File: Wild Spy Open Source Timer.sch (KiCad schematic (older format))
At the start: 36 parts, among them Q1 AO3415, Q2 AO3415, Q3 AO3415, Q4 AO3415, Q5 AO3415, U1 DS3232SN, U2 TPS70925DBVR, U3 UM6K33N, U4 UM6K33N, U5 ATXMEGA32C4-A

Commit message: Swapped to the d21 in the schematic
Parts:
- removed C3, C4, C6, C7: 0.1uF, Capacitors_SMD:C_0603_HandSoldering, symbol C_Small
- removed PDI1: CONN_01X04, MC_Footprint:PDI_PROG_HEADER, symbol CONN_01X04
- removed PortA1: CONN_01X10, Pin_Headers:Pin_Header_Straight_1x10, symbol CONN_01X10
- removed PortC1: CONN_01X10, MC_Footprint:5x2connnector_small, symbol CONN_01X10
- removed R3: 10k, Resistors_SMD:R_0603_HandSoldering, symbol R
- removed U5: ATXMEGA32C4-A, Housings_QFP:TQFP-44_10x10mm_Pitch0.8mm, symbol ATXMEGA32C4-A
- added C? (x2): 0.1uF, Capacitors_SMD:C_0603_HandSoldering, symbol C_Small
- added C?: 1uF, Capacitors_SMD:C_0603_HandSoldering, symbol C_Small
- added J?: CONN_01X05, Pin_Headers:Pin_Header_Straight_1x05_Pitch2.54mm, symbol CONN_01X05
- added J?: CONN_02X04, Pin_Headers:Pin_Header_Straight_2x04_Pitch2.54mm, symbol CONN_02X04
- added R?: 1.7k, Resistors_SMD:R_0603_HandSoldering, symbol R
- added R?: 3.3k, Resistors_SMD:R_0603_HandSoldering, symbol R
- added U?: ATSAMD21E16B, Housings_DFN_QFN:QFN-32-1EP_5x5mm_Pitch0.5mm, symbol ATSAMD21E16B
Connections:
- net labels added: NRESET, PA08, PA09, PA10, PA11, PA14, PA15, SWDCLK, SWDIO, USBSENSE3.3
- net labels removed: PA0, PA1, PA2, PA3, PA4, PA5, PA6, PA7, PC0, PC1, PC2, PC3, PC4, PC5, PC6, PC7, PDI_CLK, PDI_DATA
- wire segments 149 -> 100
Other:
- note removed: "Extra ports broken out."
- note removed: "needed?"

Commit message: - Updates to Rev1 Schematic - Organising/Tidying - Add peripheral bus port - Battery voltage measurement - Battery/USB selection jumper - Started skeleton of Rev1 PCB - Added libs folder with some footprints
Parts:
- removed Coin1: 16mm_Coin_Cell, MC_Footprint:CoinCell_Holder_1632, symbol 16mm_Coin_Cell
- added JP1: JUMPER3, jumper:SOLDER-JUMPER_2-WAY, symbol JUMPER3
- added PBus1: CONN_01X04, Pin_Headers:Pin_Header_Straight_1x04, symbol CONN_01X04
- added Q6: AO3415, TO_SOT_Packages_SMD:SOT-23, symbol Q_PMOS_GSD
- added R3: 150k, Resistors_SMD:R_0603_HandSoldering, symbol R
- added R8: 10k, Resistors_SMD:R_0603_HandSoldering, symbol R
- R4, R5, R6, R7: value 10k -> 100k
- U2: value TPS70925DBVR -> TPS70933DBVR; Supplier 1 Cost 1.1334 -> 1.19; Supplier 1 Part Number 296-40923-1-ND -> 296-35483-1-ND
- U5: renamed from U?; value ATSAMD21E16B -> ATSAMD21E18B; Manufacturer Part Number (none) -> ATSAMD21E18A-MUT; Supplier 1 (none) -> DigiKey; Supplier 1 Cost (none) -> 3.64; Supplier 1 Currency (none) -> AUD; Supplier 1 Part Number (none) -> 1611-ATSAMD21E18A-MUTCT-ND
- gave numbers to parts that had none: 7
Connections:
- net labels added: BAT+, PBus1_MRX, PBus1_MTX, VBat/12, ~BatMeasureEn
- wire segments 100 -> 123
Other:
- note added: "3.3V"
- note added: "Battery Voltage Measure"
- note added: "Breakout"
- note added: "Channels"
- note added: "Does it count if the USB is just not plugged in? Or\nis this ok as long as we have the USB set up?"
- note added: "From Datasheet:\nIf the PA24 and PA25 pins are not connected, \nit is recommended to enable a pull-up on PA24 and\nPA25 through input GPIO mode. The aim is to avoid \nan eventually extract power consumption (<1mA) \ndue to a not stable level on pad. The port PA24 and \nPA25 doesn't have Drive Strength option."
- note added: "Leave ID pin floating \nfor USB slave"
- note added: "MCU"
- note added: "Peripheral Bus"
- note added: "Power"
- note added: "Programming"
- note added: "RTC"
- note added: "SERCOM0/2[0]"
- note added: "SERCOM0/2[1]"
- note added: "SERCOM0/2[2]"
- note added: "SERCOM0/2[3]"
- note added: "SERCOM0[0]"
- note added: "SERCOM0[1]"
- note added: "SERCOM0[2]"
- note added: "SERCOM0[3]"
- note added: "SERCOM1/3[0]"
- note added: "SERCOM1/3[1]"
- note added: "SERCOM1/3[2]"
- note added: "SERCOM1/3[3]"
- note added: "SERCOM1[0]"
- note added: "SERCOM3/5[0]"
- note added: "SERCOM3/5[1]"
- note added: "SERCOM3/5[2]"
- note added: "SERCOM3/5[3]"
- note added: "USB"
- note removed: "Leave ID pin floating for USB slave"
- moved on the sheet: Battery1, Breakout, C1, C2, C3, C4, C5, C6, C8, CH1, CH2, CH3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

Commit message: PCB components placed
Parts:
- removed VUSB1: CONN_01X02, Pin_Headers:Pin_Header_Straight_1x02, symbol CONN_01X02
- added D1: LED, LEDs:LED_0603, symbol LED
- added R11: 1k, Resistors_SMD:R_0603_HandSoldering, symbol R
- Breakout1: renamed from Breakout; footprint Pin_Headers:Pin_Header_Straight_2x04_Pitch2.54mm -> MC_Footprint:4x2connnector_small
- PBus1: footprint Pin_Headers:Pin_Header_Straight_1x04 -> Pin_Headers:Pin_Header_Straight_1x04_Pitch2.54mm
- Q1, Q2, Q3, Q4, Q5, Q6: footprint TO_SOT_Packages_SMD:SOT-23 -> MC_Footprint:SOT-23-HandSoldering
- SWD1: renamed from SWD; footprint Pin_Headers:Pin_Header_Straight_1x05_Pitch2.54mm -> MC_Footprint:SWD_PROG_HEADER
- U1: footprint Housings_SOIC:SOIC-20_7.5x12.8mm_Pitch1.27mm -> Housings_SOIC:SOIC-20W_7.5x12.8mm_Pitch1.27mm
- U2: footprint TO_SOT_Packages_SMD:SOT-23-5 -> TO_SOT_Packages_SMD:SOT-23-5_HandSoldering
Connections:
- net labels added: LED, VBat/15
- net labels removed: VBat/12
- wire segments 123 -> 126
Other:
- note added: "LED Connected to PA07\n"
- moved on the sheet: C3

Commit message: Cleaned up routing on PCB a bit. Made some changes to schematic, added a few things.
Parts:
- removed Breakout1: CONN_02X04, MC_Footprint:4x2connnector_small, symbol CONN_02X04
- removed JP1: JUMPER3, jumper:SOLDER-JUMPER_2-WAY, symbol JUMPER3
- removed U5: ATSAMD21E18B, Housings_DFN_QFN:QFN-32-1EP_5x5mm_Pitch0.5mm, symbol ATSAMD21E16B
- added JP1: JUMPER3-closed, OSTFootprints:SOLDER-JUMPER_2-WAY-CLOSED, symbol JUMPER3-closed
- added SW1: SW_PUSH, OSTFootprints:KMT071NGJLHS_3x2.6mm_switch, symbol SW_PUSH
- added SW?: ORD213, OSTFootprints:ORD213S-1, symbol ORD213
- added U?: ATSAMD21E16B, OSTFootprints:QFN-32-1EP_5x5mm_Pitch0.5mm, symbol ATSAMD21E16B
- D1: symbol LED -> LED-RESCUE-Wild_Spy_Open_Source_Timer
- Q1, Q2, Q3, Q4, Q5, Q6: footprint MC_Footprint:SOT-23-HandSoldering -> OSTFootprints:SOT-23-HandSoldering
- SWD1: footprint MC_Footprint:SWD_PROG_HEADER -> OSTFootprints:SWD_PROG_HEADER
- U1: footprint Housings_SOIC:SOIC-20W_7.5x12.8mm_Pitch1.27mm -> OSTFootprints:SOIC-20_7.5x12.8mm_Pitch1.27mm
- U2: footprint TO_SOT_Packages_SMD:SOT-23-5_HandSoldering -> OSTFootprints:SOT-23-5_HandSoldering
- USB1: footprint MC_Footprint:micro_USB -> OSTFootprints:micro_USB
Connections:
- net labels added: BL_FW_UPDATE, REEDSW
- net labels removed: PA11, PA14, PA15
- wire segments 126 -> 129
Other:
- note removed: "Breakout"
- moved on the sheet: D1, R11

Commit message: Pretty much finished REV1 PCB. Just need to have a quick look over it and export gerbers etc.
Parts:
- removed JP1: JUMPER3-closed, OSTFootprints:SOLDER-JUMPER_2-WAY-CLOSED, symbol JUMPER3-closed
- added JP1: JUMPER3, OSTFootprints:SOLDER-JUMPER_2-WAY, symbol JUMPER3
- PBus1: footprint Pin_Headers:Pin_Header_Straight_1x04_Pitch2.54mm -> OSTFootprints:Pin_Header_Straight_1x04_Pitch2.54mm
- SWD1: footprint OSTFootprints:SWD_PROG_HEADER -> OSTFootprints:SWD_PROG_HEADER_L
- gave numbers to parts that had none: 2
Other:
- moved on the sheet: U3B, U4A
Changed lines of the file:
@@
 L UM6K33N U4
 U 1 1 5803421A
-P 9250 1550
-F 0 "U4" H 9450 1550 60  0000 C CNN
-F 1 "UM6K33N" H 9550 1600 60  0001 C CNN
-F 2 "MC_Footprint:SC88(SOT363)" H 9450 2050 60  0001 C CNN
-F 3 "http://rohmfs.rohm.com/en/products/databook/datasheet/discrete/transistor/mosfet/um6k33n.pdf" H 9800 2250 60  0001 C CNN
-F 4 "DigiKey" H 9350 1850 60  0001 C CNN "Supplier 1"
-F 5 "UM6K33NTNTR-ND" H 9450 1950 60  0001 C CNN "Supplier 1 Part Number"
-F 6 "$0.08638" H 9550 2050 60  0001 C CNN "Supplier 1 Cost"
-F 7 "AUD" H 9650 2150 60  0001 C CNN "Supplier 1 Currency"
-	1    9250 1550
+P 7350 2650
+F 0 "U4" H 7550 2650 60  0000 C CNN
+F 1 "UM6K33N" H 7650 2700 60  0001 C CNN
+F 2 "MC_Footprint:SC88(SOT363)" H 7550 3150 60  0001 C CNN
+F 3 "http://rohmfs.rohm.com/en/products/databook/datasheet/discrete/transistor/mosfet/um6k33n.pdf" H 7900 3350 60  0001 C CNN
+F 4 "DigiKey" H 7450 2950 60  0001 C CNN "Supplier 1"
+F 5 "UM6K33NTNTR-ND" H 7550 3050 60  0001 C CNN "Supplier 1 Part Number"
+F 6 "$0.08638" H 7650 3150 60  0001 C CNN "Supplier 1 Cost"
+F 7 "AUD" H 7750 3250 60  0001 C CNN "Supplier 1 Currency"
+	1    7350 2650
 	1    0    0    -1
 $EndComp
@@
 L UM6K33N U3
 U 2 1 580347ED
-P 7350 2650
-F 0 "U3" H 7550 2650 60  0000 C CNN
-F 1 "UM6K33N" H 7650 2700 60  0001 C CNN
-F 2 "MC_Footprint:SC88(SOT363)" H 7550 3150 60  0001 C CNN
-F 3 "http://rohmfs.rohm.com/en/products/databook/datasheet/discrete/transistor/mosfet/um6k33n.pdf" H 7900 3350 60  0001 C CNN
-F 4 "DigiKey" H 7450 2950 60  0001 C CNN "Supplier 1"
-F 5 "UM6K33NTNTR-ND" H 7550 3050 60  0001 C CNN "Supplier 1 Part Number"
-F 6 "$0.08638" H 7650 3150 60  0001 C CNN "Supplier 1 Cost"
-F 7 "AUD" H 7750 3250 60  0001 C CNN "Supplier 1 Currency"
-	2    7350 2650
+P 9250 1550
+F 0 "U3" H 9450 1550 60  0000 C CNN
+F 1 "UM6K33N" H 9550 1600 60  0001 C CNN
+F 2 "MC_Footprint:SC88(SOT363)" H 9450 2050 60  0001 C CNN
+F 3 "http://rohmfs.rohm.com/en/products/databook/datasheet/discrete/transistor/mosfet/um6k33n.pdf" H 9800 2250 60  0001 C CNN
+F 4 "DigiKey" H 9350 1850 60  0001 C CNN "Supplier 1"
+F 5 "UM6K33NTNTR-ND" H 9450 1950 60  0001 C CNN "Supplier 1 Part Number"
+F 6 "$0.08638" H 9550 2050 60  0001 C CNN "Supplier 1 Cost"
+F 7 "AUD" H 9650 2150 60  0001 C CNN "Supplier 1 Currency"
+	2    9250 1550
 	1    0    0    -1
 $EndComp
@@
 	1    0    0    -1
 $EndComp
-Text Label 5650 2500 0    60   ~ 0
+Text Label 5650 2400 0    60   ~ 0
 ~RTC_PEN
-Text Label 5650 2400 0    60   ~ 0
+Text Label 3950 2600 2    60   ~ 0
 RTC_~INT
 Text Label 5650 2100 0    60   ~ 0
@@
 F 0 "SWD1" H 2300 6650 50  0000 C CNN
 F 1 "CONN_01X05" V 2400 6350 50  0000 C CNN
-F 2 "OSTFootprints:SWD_PROG_HEADER" H 2300 6350 50  0001 C CNN
+F 2 "OSTFootprints:SWD_PROG_HEADER_L" H 2300 6350 50  0001 C CNN
 F 3 "" H 2300 6350 50  0001 C CNN
 	1    2300 6350
@@
 3.3V
 $Comp
-L +5V #PWR038
+L +5V #PWR036
 U 1 1 590F6CEC
 P 1650 3900
-F 0 "#PWR038" H 1650 3750 50  0001 C CNN
+F 0 "#PWR036" H 1650 3750 50  0001 C CNN
 F 1 "+5V" H 1650 4050 50  0000 C CNN
 F 2 "" H 1650 3900 50  0000 C CNN
@@
 Text Notes 3100 4800 0    60   ~ 12
 Does it count if the USB is just not plugged in? Or\nis this ok as long as we have the USB set up?
-Text Notes 4650 3850 1    40   ~ 0
+Text Notes 4650 3900 1    40   ~ 0
 SERCOM0/2[0]
-Text Notes 4750 3850 1    40   ~ 0
+Text Notes 4750 3900 1    40   ~ 0
 SERCOM0/2[1]
-Text Notes 4850 3850 1    40   ~ 0
+Text Notes 4850 3900 1    40   ~ 0
 SERCOM0/2[2]
-Text Notes 4950 3850 1    40   ~ 0
+Text Notes 4950 3900 1    40   ~ 0
 SERCOM0/2[3]
 Text Notes 3550 2400 2    40   ~ 0
@@
 $EndComp
 $Comp
-L GND #PWR039
+L GND #PWR037
 U 1 1 5911D86F
 P 1050 7250
-F 0 "#PWR039" H 1050 7000 50  0001 C CNN
+F 0 "#PWR037" H 1050 7000 50  0001 C CNN
 F 1 "GND" H 1050 7100 50  0000 C CNN
 F 2 "" H 1050 7250 50  0000 C CNN
@@
 Text Label 750  6950 1    60   ~ 0
 ~BatMeasureEn
-Text Label 3600 2600 0    60   ~ 0
+Text Label 3600 2700 0    60   ~ 0
 VBat/15
-Text Label 5150 1700 1    40   ~ 0
+Text Label 4950 3000 3    40   ~ 0
 ~BatMeasureEn
 Text Label 3050 5350 0    60   ~ 0
@@
 PBus1_MRX
 $Comp
-L GND #PWR040
+L GND #PWR038
 U 1 1 59136849
 P 3050 5550
-F 0 "#PWR040" H 3050 5300 50  0001 C CNN
+F 0 "#PWR038" H 3050 5300 50  0001 C CNN
 F 1 "GND" H 3050 5400 50  0000 C CNN
 F 2 "" H 3050 5550 50  0000 C CNN
@@
 $EndComp
 $Comp
-L VCC #PWR041
+L VCC #PWR039
 U 1 1 591368CC
 P 3050 5250
-F 0 "#PWR041" H 3050 5100 50  0001 C CNN
+F 0 "#PWR039" H 3050 5100 50  0001 C CNN
 F 1 "VCC" H 3050 5400 50  0000 C CNN
 F 2 "" H 3050 5250 50  0000 C CNN
@@
 F 0 "PBus1" H 2850 5650 50  0000 C CNN
 F 1 "CONN_01X04" V 2950 5400 50  0001 C CNN
-F 2 "Pin_Headers:Pin_Header_Straight_1x04_Pitch2.54mm" H 2850 5400 50  0001 C CNN
+F 2 "OSTFootprints:Pin_Header_Straight_1x04_Pitch2.54mm" H 2850 5400 50  0001 C CNN
 F 3 "" H 2850 5400 50  0000 C CNN
 	1    2850 5400
@@
 	1    0    0    -1
 $EndComp
-Text Label 3650 2700 0    60   ~ 0
+Text Label 5150 1700 1    60   ~ 0
 LED
 Wire Wire Line
@@
 	6800 3950 6800 550
 Wire Wire Line
-	3950 2700 3650 2700
+	3600 2700 3950 2700
 Wire Wire Line
 	7850 3400 7950 3400
@@
 	7100 3400 7250 3400
 $Comp
-L GND #PWR042
+L GND #PWR040
 U 1 1 5911BDB2
 P 7100 3400
-F 0 "#PWR042" H 7100 3150 50  0001 C CNN
+F 0 "#PWR040" H 7100 3150 50  0001 C CNN
 F 1 "GND" H 7100 3250 50  0000 C CNN
 F 2 "" H 7100 3400 50  0000 C CNN
@@
 $EndComp
 $Comp
-L VCC #PWR043
+L VCC #PWR041
 U 1 1 59115E50
 P 4250 3300
-F 0 "#PWR043" H 4250 3150 50  0001 C CNN
+F 0 "#PWR041" H 4250 3150 50  0001 C CNN
 F 1 "VCC" H 4250 3450 50  0000 C CNN
 F 2 "" H 4250 3300 50  0000 C CNN
@@
 Wire Wire Line
 	4450 3300 4250 3300
-Connection ~ 4450 3300
-$Comp
-L ATSAMD21E16B U?
+$Comp
+L ATSAMD21E16B U5
 U 1 1 5914505E
 P 4750 2400
-F 0 "U?" H 4200 2950 60  0000 C CNN
+F 0 "U5" H 4200 2950 60  0000 C CNN
 F 1 "ATSAMD21E16B" H 5500 1950 60  0000 C CNN
 F 2 "OSTFootprints:QFN-32-1EP_5x5mm_Pitch0.5mm" H 4100 2850 60  0001 C CNN
@@
 	1    4750 2400
 	1    0    0    -1
-$EndComp
-$Comp
-L JUMPER3-closed JP1
-U 1 1 59145DE3
-P 1900 3900
-F 0 "JP1" H 1700 3800 50  0000 L CNN
-F 1 "JUMPER3-closed" H 1900 4000 50  0000 C BNN
-F 2 "OSTFootprints:SOLDER-JUMPER_2-WAY-CLOSED" H 1850 3700 50  0001 C CNN
-F 3 "" H 1900 3900 50  0000 C CNN
-	1    1900 3900
-	-1   0    0    -1
 $EndComp
 $Comp
@@
 $EndComp
 $Comp
-L GND #PWR?
+L GND #PWR042
 U 1 1 59143C7E
 P 8300 3900
-F 0 "#PWR?" H 8300 3650 50  0001 C CNN
+F 0 "#PWR042" H 8300 3650 50  0001 C CNN
 F 1 "GND" H 8300 3750 50  0000 C CNN
 F 2 "" H 8300 3900 50  0000 C CNN
@@
 BL_FW_UPDATE
 $Comp
-L ORD213 SW?
+L ORD213 SW2
 U 1 1 59147387
 P 7950 4350
-F 0 "SW?" H 7950 4450 50  0000 C CNN
+F 0 "SW2" H 7950 4450 50  0000 C CNN
 F 1 "ORD213" H 7950 4250 50  0000 C CNN
 F 2 "OSTFootprints:ORD213S-1" H 8380 4690 60  0001 C CNN
@@
 $EndComp
 $Comp
-L GND #PWR?
+L GND #PWR043
 U 1 1 59148235
 P 8250 4350
-F 0 "#PWR?" H 8250 4100 50  0001 C CNN
+F 0 "#PWR043" H 8250 4100 50  0001 C CNN
 F 1 "GND" H 8250 4200 50  0000 C CNN
 F 2 "" H 8250 4350 50  0000 C CNN
@@
 Wire Wire Line
 	7450 4350 7850 4350
-Text Label 4950 3000 3    60   ~ 0
+Text Label 6000 2500 2    60   ~ 0
 REEDSW
+$Comp
+L JUMPER3 JP1
+U 1 1 5914F4EF
+P 1900 3900
+F 0 "JP1" H 1950 3800 50  0000 L CNN
+F 1 "JUMPER3" H 1900 4000 50  0000 C BNN
+F 2 "OSTFootprints:SOLDER-JUMPER_2-WAY" H 1900 3900 50  0001 C CNN
+F 3 "" H 1900 3900 50  0000 C CNN
+	1    1900 3900
+	1    0    0    -1
+$EndComp
+Connection ~ 4450 3300
 $EndSCHEMATC

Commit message: Finished the PCB layout
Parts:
- D1: footprint LEDs:LED_0603 -> OSTFootprints:LED_0603
- U3, U4: footprint MC_Footprint:SC88(SOT363) -> OSTFootprints:SC88(SOT363)
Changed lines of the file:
@@
 F 0 "U3" H 7550 1550 60  0000 C CNN
 F 1 "UM6K33N" H 7650 1600 60  0001 C CNN
-F 2 "MC_Footprint:SC88(SOT363)" H 7550 2050 60  0001 C CNN
+F 2 "OSTFootprints:SC88(SOT363)" H 7550 2050 60  0001 C CNN
 F 3 "http://rohmfs.rohm.com/en/products/databook/datasheet/discrete/transistor/mosfet/um6k33n.pdf" H 7900 2250 60  0001 C CNN
 F 4 "DigiKey" H 7450 1850 60  0001 C CNN "Supplier 1"
@@
 F 0 "U4" H 7550 2650 60  0000 C CNN
 F 1 "UM6K33N" H 7650 2700 60  0001 C CNN
-F 2 "MC_Footprint:SC88(SOT363)" H 7550 3150 60  0001 C CNN
+F 2 "OSTFootprints:SC88(SOT363)" H 7550 3150 60  0001 C CNN
 F 3 "http://rohmfs.rohm.com/en/products/databook/datasheet/discrete/transistor/mosfet/um6k33n.pdf" H 7900 3350 60  0001 C CNN
 F 4 "DigiKey" H 7450 2950 60  0001 C CNN "Supplier 1"
@@
 F 0 "U3" H 9450 1550 60  0000 C CNN
 F 1 "UM6K33N" H 9550 1600 60  0001 C CNN
-F 2 "MC_Footprint:SC88(SOT363)" H 9450 2050 60  0001 C CNN
+F 2 "OSTFootprints:SC88(SOT363)" H 9450 2050 60  0001 C CNN
 F 3 "http://rohmfs.rohm.com/en/products/databook/datasheet/discrete/transistor/mosfet/um6k33n.pdf" H 9800 2250 60  0001 C CNN
 F 4 "DigiKey" H 9350 1850 60  0001 C CNN "Supplier 1"
@@
 F 0 "U4" H 9450 2650 60  0000 C CNN
 F 1 "UM6K33N" H 9550 2700 60  0001 C CNN
-F 2 "MC_Footprint:SC88(SOT363)" H 9450 3150 60  0001 C CNN
+F 2 "OSTFootprints:SC88(SOT363)" H 9450 3150 60  0001 C CNN
 F 3 "http://rohmfs.rohm.com/en/products/databook/datasheet/discrete/transistor/mosfet/um6k33n.pdf" H 9800 3350 60  0001 C CNN
 F 4 "DigiKey" H 9350 2950 60  0001 C CNN "Supplier 1"
@@
 F 0 "D1" H 7400 3500 50  0000 C CNN
 F 1 "LED" H 7400 3300 50  0000 C CNN
-F 2 "LEDs:LED_0603" H 7400 3400 50  0001 C CNN
+F 2 "OSTFootprints:LED_0603" H 7400 3400 50  0001 C CNN
 F 3 "" H 7400 3400 50  0001 C CNN
 	1    7400 3400

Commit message: Generated Gerbers for Rev1 Generated BOM for Rev1 Generated renders for Rev1 Some updating of paths and libs
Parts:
- Battery1, CH1, CH2, CH3, CH4, JP1, PBus1, SWD1: fit_field (none) -> dnf
- R10: value 3.3k -> 2k
- R9: value 1.7k -> 1k
- SW1: Supplier 1 (none) -> DigiKey; Supplier 1 Cost (none) -> 0.39; Supplier 1 Currency (none) -> AUD; Supplier 1 Part Number (none) -> CKN10291CT-ND
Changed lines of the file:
@@
 F 2 "Pin_Headers:Pin_Header_Straight_1x02" H 750 3200 50  0001 C CNN
 F 3 "" H 750 3200 50  0000 C CNN
+F 4 "dnf" V 750 3200 60  0001 C CNN "fit_field"
 	1    750  3200
 	0    -1   -1   0
@@
 F 2 "Pin_Headers:Pin_Header_Straight_1x03" H 8650 1400 50  0001 C CNN
 F 3 "" H 8650 1400 50  0000 C CNN
+F 4 "dnf" H 8650 1400 60  0001 C CNN "fit_field"
 	1    8650 1400
 	1    0    0    -1
@@
 F 2 "Pin_Headers:Pin_Header_Straight_1x03" H 10550 1400 50  0001 C CNN
 F 3 "" H 10550 1400 50  0000 C CNN
+F 4 "dnf" H 10550 1400 60  0001 C CNN "fit_field"
 	1    10550 1400
 	1    0    0    -1
@@
 F 2 "Pin_Headers:Pin_Header_Straight_1x03" H 8650 2500 50  0001 C CNN
 F 3 "" H 8650 2500 50  0000 C CNN
+F 4 "dnf" H 8650 2500 60  0001 C CNN "fit_field"
 	1    8650 2500
 	1    0    0    -1
@@
 F 2 "Pin_Headers:Pin_Header_Straight_1x03" H 10550 2500 50  0001 C CNN
 F 3 "" H 10550 2500 50  0000 C CNN
+F 4 "dnf" H 10550 2500 60  0001 C CNN "fit_field"
 	1    10550 2500
 	1    0    0    -1
@@
 P 2050 4950
 F 0 "R9" V 2130 4950 50  0000 C CNN
-F 1 "1.7k" V 2050 4950 50  0000 C CNN
+F 1 "1k" V 2050 4950 50  0000 C CNN
 F 2 "Resistors_SMD:R_0603_HandSoldering" V 1980 4950 50  0001 C CNN
 F 3 "" H 2050 4950 50  0000 C CNN
@@
 P 2050 5250
 F 0 "R10" V 2130 5250 50  0000 C CNN
-F 1 "3.3k" V 2050 5250 50  0000 C CNN
+F 1 "2k" V 2050 5250 50  0000 C CNN
 F 2 "Resistors_SMD:R_0603_HandSoldering" V 1980 5250 50  0001 C CNN
 F 3 "" H 2050 5250 50  0000 C CNN
@@
 F 2 "OSTFootprints:SWD_PROG_HEADER_L" H 2300 6350 50  0001 C CNN
 F 3 "" H 2300 6350 50  0001 C CNN
+F 4 "dnf" H 2300 6350 60  0001 C CNN "fit_field"
 	1    2300 6350
 	1    0    0    -1
@@
 F 2 "OSTFootprints:Pin_Header_Straight_1x04_Pitch2.54mm" H 2850 5400 50  0001 C CNN
 F 3 "" H 2850 5400 50  0000 C CNN
+F 4 "dnf" H 2850 5400 60  0001 C CNN "fit_field"
 	1    2850 5400
 	-1   0    0    1
@@
 F 2 "OSTFootprints:KMT071NGJLHS_3x2.6mm_switch" H 7900 3900 50  0001 C CNN
 F 3 "" H 7900 3900 50  0000 C CNN
+F 4 "DigiKey" H 7900 3900 60  0001 C CNN "Supplier 1"
+F 5 "CKN10291CT-ND" H 7900 3900 60  0001 C CNN "Supplier 1 Part Number"
+F 6 "0.39" H 7900 3900 60  0001 C CNN "Supplier 1 Cost"
+F 7 "AUD" H 7900 3900 60  0001 C CNN "Supplier 1 Currency"
 	1    7900 3900
 	1    0    0    -1
@@
 F 2 "OSTFootprints:SOLDER-JUMPER_2-WAY" H 1900 3900 50  0001 C CNN
 F 3 "" H 1900 3900 50  0000 C CNN
+F 4 "dnf" H 1900 3900 60  0001 C CNN "fit_field"
 	1    1900 3900
 	1    0    0    -1

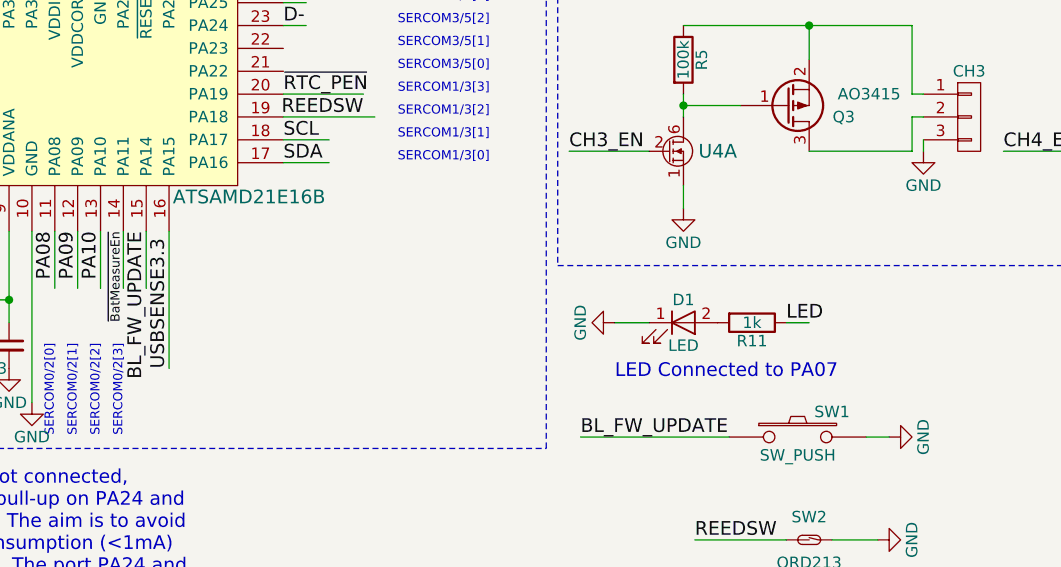
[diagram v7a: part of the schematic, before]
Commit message: Removed Harry's commit of WavTriggerBoard.  Should not be in this repo. Updated chip in schematic.
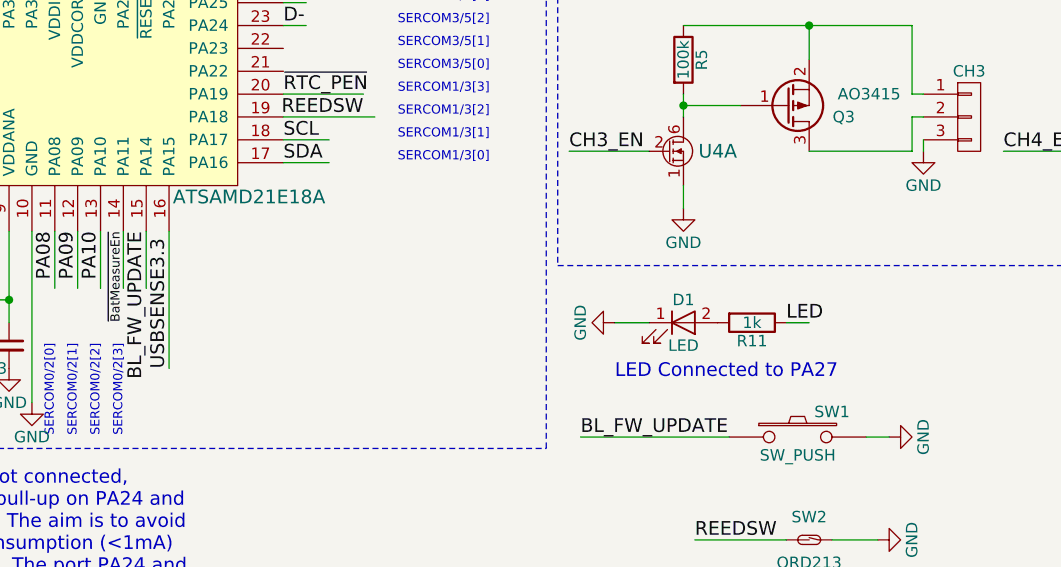
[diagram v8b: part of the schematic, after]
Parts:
- U5: value ATSAMD21E16B -> ATSAMD21E18A
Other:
- note added: "LED Connected to PA27\n"
- note removed: "LED Connected to PA07\n"
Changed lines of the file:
@@
 LED
 Text Notes 7100 3650 0    60   ~ 0
-LED Connected to PA07\n
+LED Connected to PA27\n
 Wire Wire Line
 	7100 3400 7250 3400
@@
 P 4750 2400
 F 0 "U5" H 4200 2950 60  0000 C CNN
-F 1 "ATSAMD21E16B" H 5500 1950 60  0000 C CNN
+F 1 "ATSAMD21E18A" H 5500 1950 60  0000 C CNN
 F 2 "OSTFootprints:QFN-32-1EP_5x5mm_Pitch0.5mm" H 4100 2850 60  0001 C CNN
 F 3 "http://www.atmel.com/Images/Atmel-42181-SAM-D21_Datasheet.pdf" H 4200 2950 60  0001 C CNN
